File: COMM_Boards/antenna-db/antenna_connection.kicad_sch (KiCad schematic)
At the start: 8 parts

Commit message: COMM: antt-dbd: map mounting holes to pcb layout
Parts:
- gave numbers to parts that had none: 8
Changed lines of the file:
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@@
   (symbol (lib_id "Connector:Conn_Coaxial") (at 106.68 53.34 180) (unit 1)
     (in_bom yes) (on_board yes) (fields_autoplaced)
-    (property "Reference" "J?" (id 0) (at 102.87 51.7767 0)
+    (property "Reference" "J5" (id 0) (at 102.87 51.7767 0)
       (effects (font (size 1.27 1.27)) (justify left))
     )
@@
   (symbol (lib_id "Connector:TestPoint") (at 207.01 53.34 270) (unit 1)
     (in_bom yes) (on_board yes) (fields_autoplaced)
-    (property "Reference" "TP?" (id 0) (at 212.09 52.0699 90)
+    (property "Reference" "TP5" (id 0) (at 212.09 52.0699 90)
       (effects (font (size 1.27 1.27)) (justify left))
     )
@@
   (symbol (lib_id "Connector:Conn_Coaxial") (at 107.95 114.3 180) (unit 1)
     (in_bom yes) (on_board yes) (fields_autoplaced)
-    (property "Reference" "J?" (id 0) (at 104.14 112.7367 0)
+    (property "Reference" "J6" (id 0) (at 104.14 112.7367 0)
       (effects (font (size 1.27 1.27)) (justify left))
     )
@@
   (symbol (lib_id "Connector:TestPoint") (at 208.28 119.38 270) (unit 1)
     (in_bom yes) (on_board yes) (fields_autoplaced)
-    (property "Reference" "TP?" (id 0) (at 213.36 118.1099 90)
+    (property "Reference" "TP8" (id 0) (at 213.36 118.1099 90)
       (effects (font (size 1.27 1.27)) (justify left))
     )
@@
   (symbol (lib_id "dk_Balun:MABA-007159-000000") (at 135.89 55.88 0) (unit 1)
     (in_bom yes) (on_board yes) (fields_autoplaced)
-    (property "Reference" "T?" (id 0) (at 135.89 45.72 0)
+    (property "Reference" "T1" (id 0) (at 135.89 45.72 0)
       (effects (font (size 1.524 1.524)))
     )
@@
   (symbol (lib_id "Connector:TestPoint") (at 207.01 58.42 270) (unit 1)
     (in_bom yes) (on_board yes) (fields_autoplaced)
-    (property "Reference" "TP?" (id 0) (at 212.09 57.1499 90)
+    (property "Reference" "TP6" (id 0) (at 212.09 57.1499 90)
       (effects (font (size 1.27 1.27)) (justify left))
     )
@@
   (symbol (lib_id "power:GND") (at 121.92 123.19 0) (unit 1)
     (in_bom yes) (on_board yes) (fields_autoplaced)
-    (property "Reference" "#PWR?" (id 0) (at 121.92 129.54 0)
+    (property "Reference" "#PWR0123" (id 0) (at 121.92 129.54 0)
       (effects (font (size 1.27 1.27)) hide)
     )
@@
   (symbol (lib_id "Connector:TestPoint") (at 208.28 114.3 270) (unit 1)
     (in_bom yes) (on_board yes) (fields_autoplaced)
-    (property "Reference" "TP?" (id 0) (at 213.36 113.0299 90)
+    (property "Reference" "TP7" (id 0) (at 213.36 113.0299 90)
       (effects (font (size 1.27 1.27)) (justify left))
     )
@@
   (symbol (lib_id "dk_Balun:MABA-007159-000000") (at 137.16 116.84 0) (unit 1)
     (in_bom yes) (on_board yes) (fields_autoplaced)
-    (property "Reference" "T?" (id 0) (at 137.16 106.68 0)
+    (property "Reference" "T2" (id 0) (at 137.16 106.68 0)
       (effects (font (size 1.524 1.524)))
     )
@@
   (symbol (lib_id "power:GND") (at 120.65 62.23 0) (unit 1)
     (in_bom yes) (on_board yes) (fields_autoplaced)
-    (property "Reference" "#PWR?" (id 0) (at 120.65 68.58 0)
-      (effects (font (size 1.27 1.27)) hide)
-    )
+    (property "Reference" "#PWR0122" (id 0) (at 120.65 68.58 0)
+      (effects (font (size 1.27 1.27)) hide)
+    )

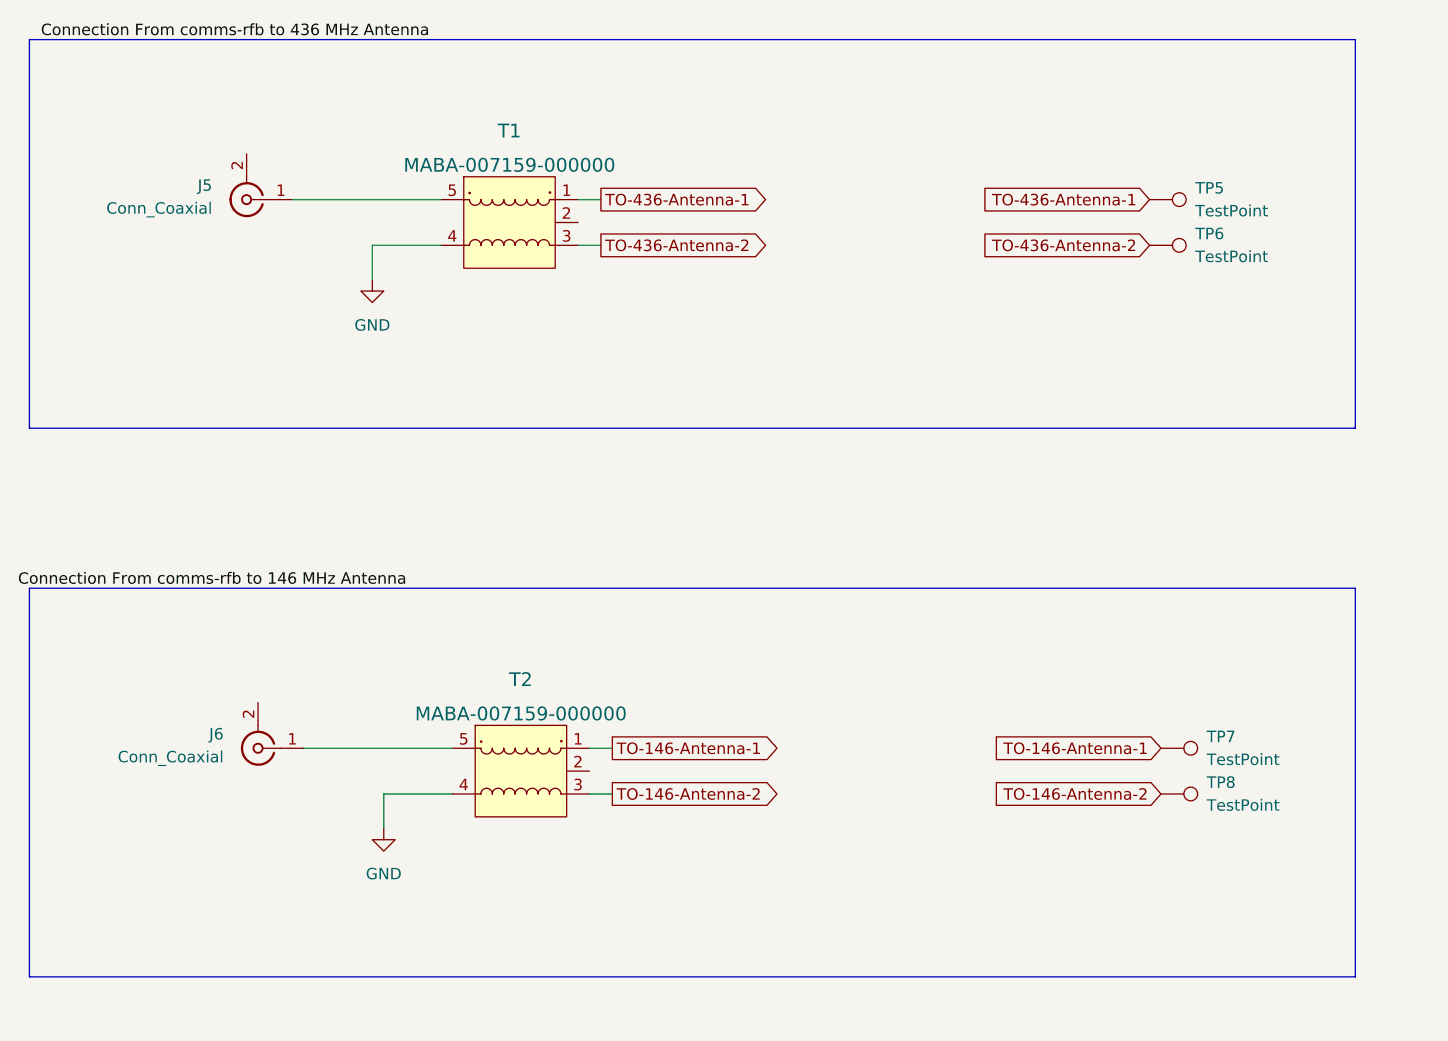
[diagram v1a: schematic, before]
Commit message: include SC4216 regulator
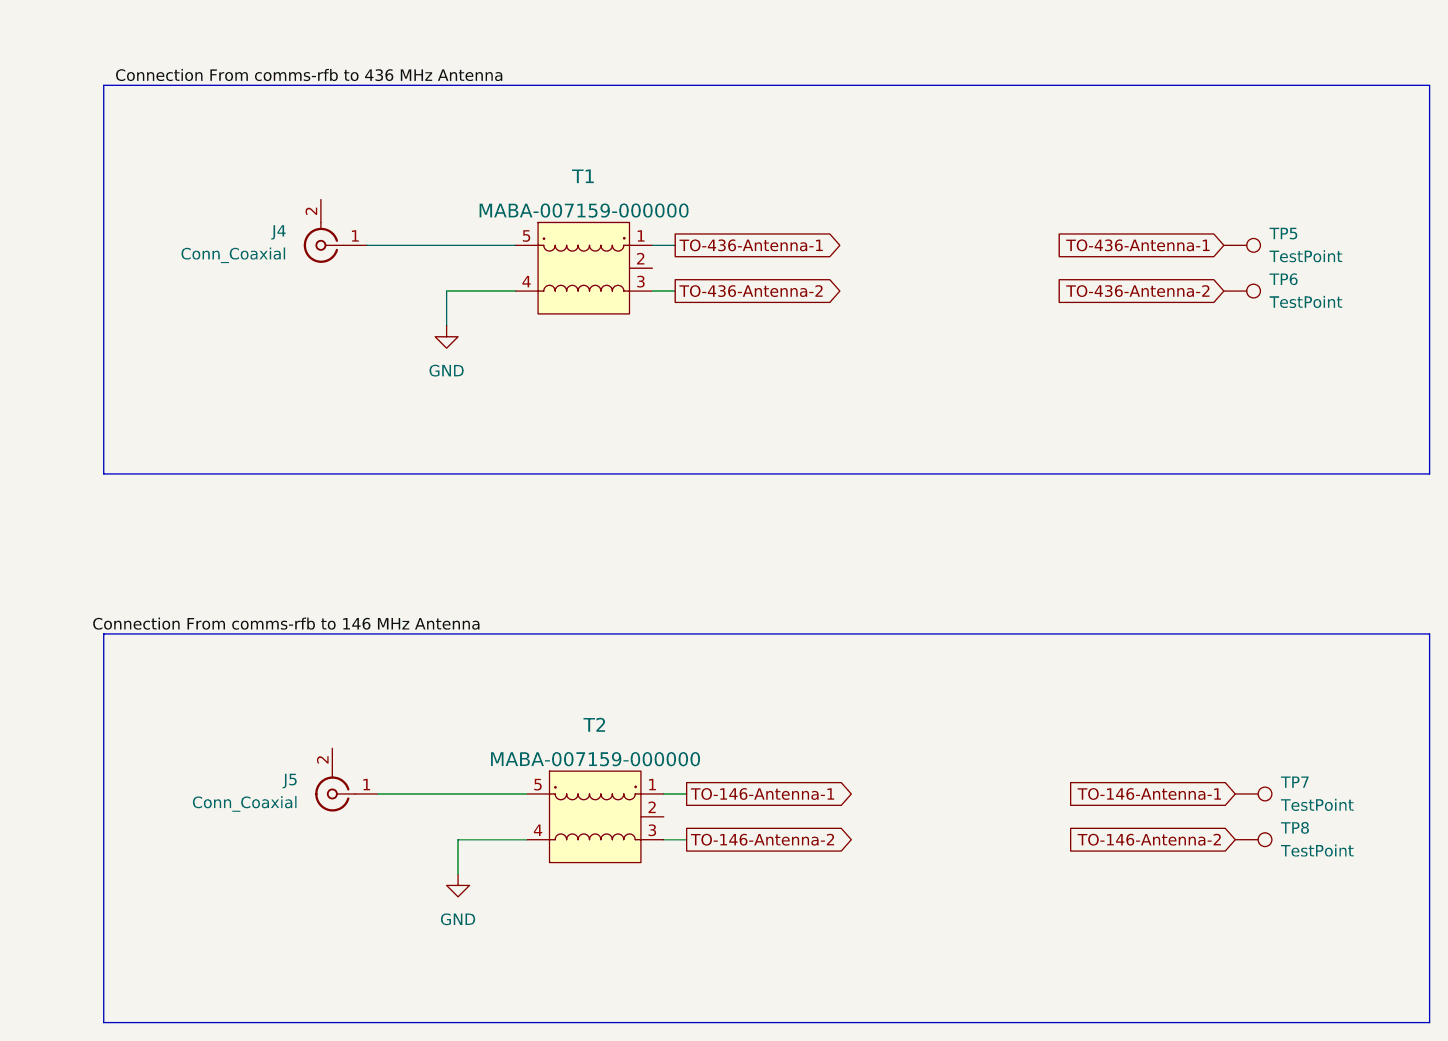
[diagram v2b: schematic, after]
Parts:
- removed J6: Conn_Coaxial, symbol Connector:Conn_Coaxial
- added J4: Conn_Coaxial, TestPoint:TestPoint_THTPad_4.0x4.0mm_Drill2.0mm, symbol Connector:Conn_Coaxial
- J5, TP5, TP6, TP7, TP8: footprint (none) -> TestPoint:TestPoint_THTPad_4.0x4.0mm_Drill2.0mm
- T1, T2: footprint digikey-footprints:SMD-5-6_3.83x2.79mm -> qset-footprints:MABA-007159-000000
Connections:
- net at J5.1 (In): now also T2.5; no longer T1.5
- new net: J4.1 (In), T1.5

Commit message: COMM: antt-dbd: finish deployment detection and arming control
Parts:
- removed J4, J5: Conn_Coaxial, TestPoint:TestPoint_THTPad_4.0x4.0mm_Drill2.0mm, symbol Connector:Conn_Coaxial
- removed T1, T2: MABA-007159-000000, qset-footprints:MABA-007159-000000, symbol dk_Balun:MABA-007159-000000
- removed TP5, TP6, TP7, TP8: TestPoint, TestPoint:TestPoint_THTPad_4.0x4.0mm_Drill2.0mm, symbol Connector:TestPoint
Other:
- company: (none) -> Queen's Space Engineering Team - Satellite
- title: (none) -> Antenna Deployment Board
